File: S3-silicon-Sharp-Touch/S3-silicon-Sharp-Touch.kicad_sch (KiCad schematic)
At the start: 63 parts, among them IC1 ESP32-S3FN8, J2 Conn_01x06_Socket, J3 Conn_01x11_Socket, J5 FH52-10S-0.5SH_99, J6 5024260810, J7 S2B-PH-SM4-TB_LF__SN_, J9 USB_C_Receptacle_USB2.0, Q3 MMBT3904, Q3 Si2301CDS, Q4 MMBT3904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

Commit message: Heading for Rel 1.1
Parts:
- added J4: SM04B-SRSS-TB_LF__SN_, foot_sharp:QWIIC_SM04B-SRSS-TB_LFSN_, symbol QWIIC:SM04B-SRSS-TB_LF__SN_
- D8: value LED -> LED GREEN
- D9: value LED -> LED RED
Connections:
- net GND: now also J7.1, J4.4; no longer J7.2
- net SCL: now also J4.1
- net SDA: now also J4.2
- net VBAT: now also J7.2; no longer J7.1
- net VDD33: now also J4.3
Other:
- note added: "QWIIC I2C Connector"
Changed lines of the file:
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@@
     (stroke (width 0) (type default))
   )
+  (wire (pts (xy 344.17 106.68) (xy 336.55 106.68))
+    (stroke (width 0) (type default))
+  )
   (wire (pts (xy 336.55 166.37) (xy 340.36 166.37))
     (stroke (width 0) (type default))
@@
     (stroke (width 0) (type default))
   )
+  (wire (pts (xy 344.17 110.49) (xy 344.17 106.68))
+    (stroke (width 0) (type default))
+  )
   (wire (pts (xy 156.21 97.79) (xy 161.29 97.79))
     (stroke (width 0) (type default))
@@
     (stroke (width 0) (type default))
   )
+  (wire (pts (xy 264.16 229.87) (xy 264.16 228.6))
+    (stroke (width 0) (type default))
+  )
   (wire (pts (xy 85.09 147.32) (xy 85.09 149.86))
     (stroke (width 0) (type default))
@@
     (stroke (width 0) (type default))
   )
+  (rectangle (start 233.68 209.55) (end 316.23 242.57)
+    (stroke (width 0) (type default))
+    (fill (type none))
+  )
   (rectangle (start 318.77 146.05) (end 383.54 199.39)
     (stroke (width 0) (type default))
@@
     (effects (font (size 1.27 1.27)) (justify left bottom))
   )
+  (text "QWIIC I2C Connector" (at 234.95 208.28 0)
+    (effects (font (size 1.27 1.27)) (justify left bottom))
+  )
   (text "R2 intentionally\nNOT placed" (at 45.72 119.38 0)
     (effects (font (size 1.27 1.27)) (justify left bottom))
@@
     (effects (font (size 0.9 0.9)) (justify left bottom))
   )
-  (text "10 FPC SHARP LCD connector" (at 252.73 146.05 0)
-    (effects (font (size 2 2)) (justify left bottom))
+  (text "10 FPC SHARP LCD connector" (at 236.22 144.78 0)
+    (effects (font (size 1.27 1.27) (thickness 0.254) bold) (justify left bottom))
   )
   (text "RC delay" (at 156.21 93.98 0)
@@
     (effects (font (size 1.27 1.27) (thickness 0.254) bold (color 0 194 0 1)) (justify right bottom))
   )
+  (label "SDA" (at 264.16 223.52 180) (fields_autoplaced)
+    (effects (font (size 1.27 1.27)) (justify right bottom))
+  )
   (label "RTC_SQW" (at 97.79 48.26 0) (fields_autoplaced)
     (effects (font (size 1.27 1.27)) (justify left bottom))
@@
     (effects (font (size 1.27 1.27)) (justify right bottom))
   )
+  (label "SCL" (at 264.16 220.98 180) (fields_autoplaced)
+    (effects (font (size 1.27 1.27)) (justify right bottom))
+  )
   (label "LCD_EXTMODE" (at 273.05 175.26 180) (fields_autoplaced)
     (effects (font (size 1.27 1.27) (thickness 0.254) bold (color 72 72 72 1)) (justify right bottom))
@@
     )
   )
-  (global_label "VBAT" (shape input) (at 336.55 106.68 0) (fields_autoplaced)
-    (effects (font (size 1.27 1.27)) (justify left))
-    (property "Intersheetrefs" "${INTERSHEET_REFS}" (at 343.95 106.68 0)
-      (effects (font (size 1.27 1.27)) (justify left) hide)
-    )
-  )
   (global_label "VBUS" (shape input) (at 309.88 48.26 180) (fields_autoplaced)
     (effects (font (size 1.27 1.27)) (justify right))
@@
     )
   )
+  (global_label "VDD33" (shape input) (at 264.16 226.06 180) (fields_autoplaced)
+    (effects (font (size 1.27 1.27)) (justify right))
+    (property "Intersheetrefs" "${INTERSHEET_REFS}" (at 255.1272 226.06 0)
+      (effects (font (size 1.27 1.27)) (justify right) hide)
+    )
+    (property "Referenzen zwischen Schaltplänen" "${INTERSHEET_REFS}" (at 264.16 228.2508 0)
+      (effects (font (size 1.27 1.27)) (justify right) hide)
+    )
+  )
   (global_label "VDD33" (shape input) (at 87.63 78.74 0) (fields_autoplaced)
     (effects (font (size 1.27 1.27)) (justify left))
@@
     )
   )
+  (global_label "VBAT" (shape input) (at 336.55 109.22 0) (fields_autoplaced)
+    (effects (font (size 1.27 1.27)) (justify left))
+    (property "Intersheetrefs" "${INTERSHEET_REFS}" (at 343.95 109.22 0)
+      (effects (font (size 1.27 1.27)) (justify left) hide)
+    )
+  )
   (global_label "VBAT" (shape input) (at 323.85 69.85 180) (fields_autoplaced)
     (effects (font (size 1.27 1.27)) (justify right))
@@
       (effects (font (size 1.27 1.27)) (justify right))
     )
-    (property "Value" "LED" (at 275.59 90.17 0)
+    (property "Value" "LED GREEN" (at 275.59 90.17 0)
       (effects (font (size 1.27 1.27) (color 0 132 0 1)) (justify right))
     )
@@
       (effects (font (size 1.27 1.27)) (justify right))
     )
-    (property "Value" "LED" (at 275.59 97.79 0)
+    (property "Value" "LED RED" (at 275.59 97.79 0)
       (effects (font (size 1.27 1.27) (color 194 0 0 1)) (justify right))
     )
@@
     )
   )
+  (symbol (lib_id "power:GND") (at 264.16 229.87 0) (unit 1)
+    (in_bom yes) (on_board yes) (dnp no)
+    (property "Reference" "#PWR034" (at 264.16 236.22 0)
+      (effects (font (size 1.27 1.27)) hide)
+    )
+    (property "Value" "GND" (at 264.287 234.2642 0)
+      (effects (font (size 1.27 1.27)))
+    )
+    (property "Footprint" "" (at 264.16 229.87 0)
+      (effects (font (size 1.27 1.27)) hide)
+    )
+    (property "Datasheet" "" (at 264.16 229.87 0)
+      (effects (font (size 1.27 1.27)) hide)
+    )
+    (pin "1")
+    (instances
+      (project "S3-silicon-Sharp-Touch"
+        (path "/e6751642-eada-4b92-b3bd-08d265514654"
+          (reference "#PWR034") (unit 1)
+        )
+      )
+    )
+  )
   (symbol (lib_id "power:GND") (at 167.64 82.55 0) (unit 1)
     (in_bom yes) (on_board yes) (dnp no) (fields_autoplaced)
@@
     )
   )
+  (symbol (lib_id "QWIIC:SM04B-SRSS-TB_LF__SN_") (at 264.16 220.98 0) (unit 1)
+    (in_bom yes) (on_board yes) (dnp no) (fields_autoplaced)
+    (property "Reference" "J4" (at 280.162 222.9429 0)
+      (effects (font (size 1.27 1.27)) (justify left))
+    )
+    (property "Value" "SM04B-SRSS-TB_LF__SN_" (at 280.162 225.3671 0)
+      (effects (font (size 1.27 1.27)) (justify left))
+    )
+    (property "Footprint" "foot_sharp:QWIIC_SM04B-SRSS-TB_LFSN_" (at 280.67 315.9 0)
+      (effects (font (size 1.27 1.27)) (justify left top) hide)
+    )
+    (property "Datasheet" "http://www.jst-mfg.com/product/pdf/eng/eSH.pdf" (at 280.67 415.9 0)
+      (effects (font (size 1.27 1.27)) (justify left top) hide)
+    )
+    (property "Height" "" (at 280.67 615.9 0)
+      (effects (font (size 1.27 1.27)) (justify left top) hide)
+    )
+    (property "Manufacturer_Name" "JST (JAPAN SOLDERLESS TERMINALS)" (at 280.67 715.9 0)
+      (effects (font (size 1.27 1.27)) (justify left top) hide)
+    )
+    (property "Manufacturer_Part_Number" "SM04B-SRSS-TB(LF)(SN)" (at 280.67 815.9 0)
+      (effects (font (size 1.27 1.27)) (justify left top) hide)
+    )
+    (property "Mouser Part Number" "" (at 280.67 915.9 0)
+      (effects (font (size 1.27 1.27)) (justify left top) hide)
+    )
+    (property "Mouser Price/Stock" "" (at 280.67 1015.9 0)
+      (effects (font (size 1.27 1.27)) (justify left top) hide)
+    )
+    (property "Arrow Part Number" "SM04B-SRSS-TB(LF)(SN)" (at 280.67 1115.9 0)
+      (effects (font (size 1.27 1.27)) (justify left top) hide)
+    )
+    (property "Arrow Price/Stock" "https://www.arrow.com/en/products/sm04b-srss-tb-lf-sn/jst-manufacturing?region=europe" (at 280.67 1215.9 0)
+      (effects (font (size 1.27 1.27)) (justify left top) hide)
+    )
+    (property "LCSC" "C160404" (at 264.16 220.98 90)
+      (effects (font (size 1.27 1.27)) hide)
+    )
+    (pin "4")
+    (pin "2")
+    (pin "3")
+    (pin "1")
+    (pin "6")
+    (pin "5")
+    (instances
+      (project "S3-silicon-Sharp-Touch"
+        (path "/e6751642-eada-4b92-b3bd-08d265514654"
+          (reference "J4") (unit 1)
+        )
+      )
+    )
+  )
   (symbol (lib_id "Device:R") (at 115.57 156.21 270) (unit 1)
     (in_bom yes) (on_board yes) (dnp no)
@@
     )
   )
+  (symbol (lib_id "power:GND") (at 344.17 110.49 0) (unit 1)
+    (in_bom yes) (on_board yes) (dnp no) (fields_autoplaced)
+    (property "Reference" "#PWR05" (at 344.17 116.84 0)
+      (effects (font (size 1.27 1.27)) hide)
+    )
+    (property "Value" "GND" (at 344.17 115.0525 0)
+      (effects (font (size 1.27 1.27)))
+    )
+    (property "Footprint" "" (at 344.17 110.49 0)
+      (effects (font (size 1.27 1.27)) hide)
+    )
+    (property "Datasheet" "" (at 344.17 110.49 0)
+      (effects (font (size 1.27 1.27)) hide)
+    )
+    (pin "1")
+    (instances
+      (project "S3-silicon-Sharp-Touch"
+        (path "/e6751642-eada-4b92-b3bd-08d265514654"
+          (reference "#PWR05") (unit 1)
+        )
+      )
+    )
+  )
   (symbol (lib_id "power:GND") (at 265.43 179.07 0) (unit 1)
     (in_bom yes) (on_board yes) (dnp no) (fields_autoplaced)
@@
         )
       )
-    )
-  )
-  (symbol (lib_id "power:GND") (at 336.55 109.22 0) (unit 1)
-    (in_bom yes) (on_board yes) (dnp no) (fields_autoplaced)
-    (property "Reference" "#PWR034" (at 336.55 115.57 0)
-      (effects (font (size 1.27 1.27)) hide)
-    )
-    (property "Value" "GND" (at 336.55 113.7825 0)
-      (effects (font (size 1.27 1.27)))
-    )
-    (property "Footprint" "" (at 336.55 109.22 0)
-      (effects (font (size 1.27 1.27)) hide)
-    )
-    (property "Datasheet" "" (at 336.55 109.22 0)
-      (effects (font (size 1.27 1.27)) hide)
-    )
-    (pin "1")
-    (instances
-      (project "S3-silicon-Sharp-Touch"
-        (path "/e6751642-eada-4b92-b3bd-08d265514654"
-          (reference "#PWR034") (unit 1)
-        )
-      )

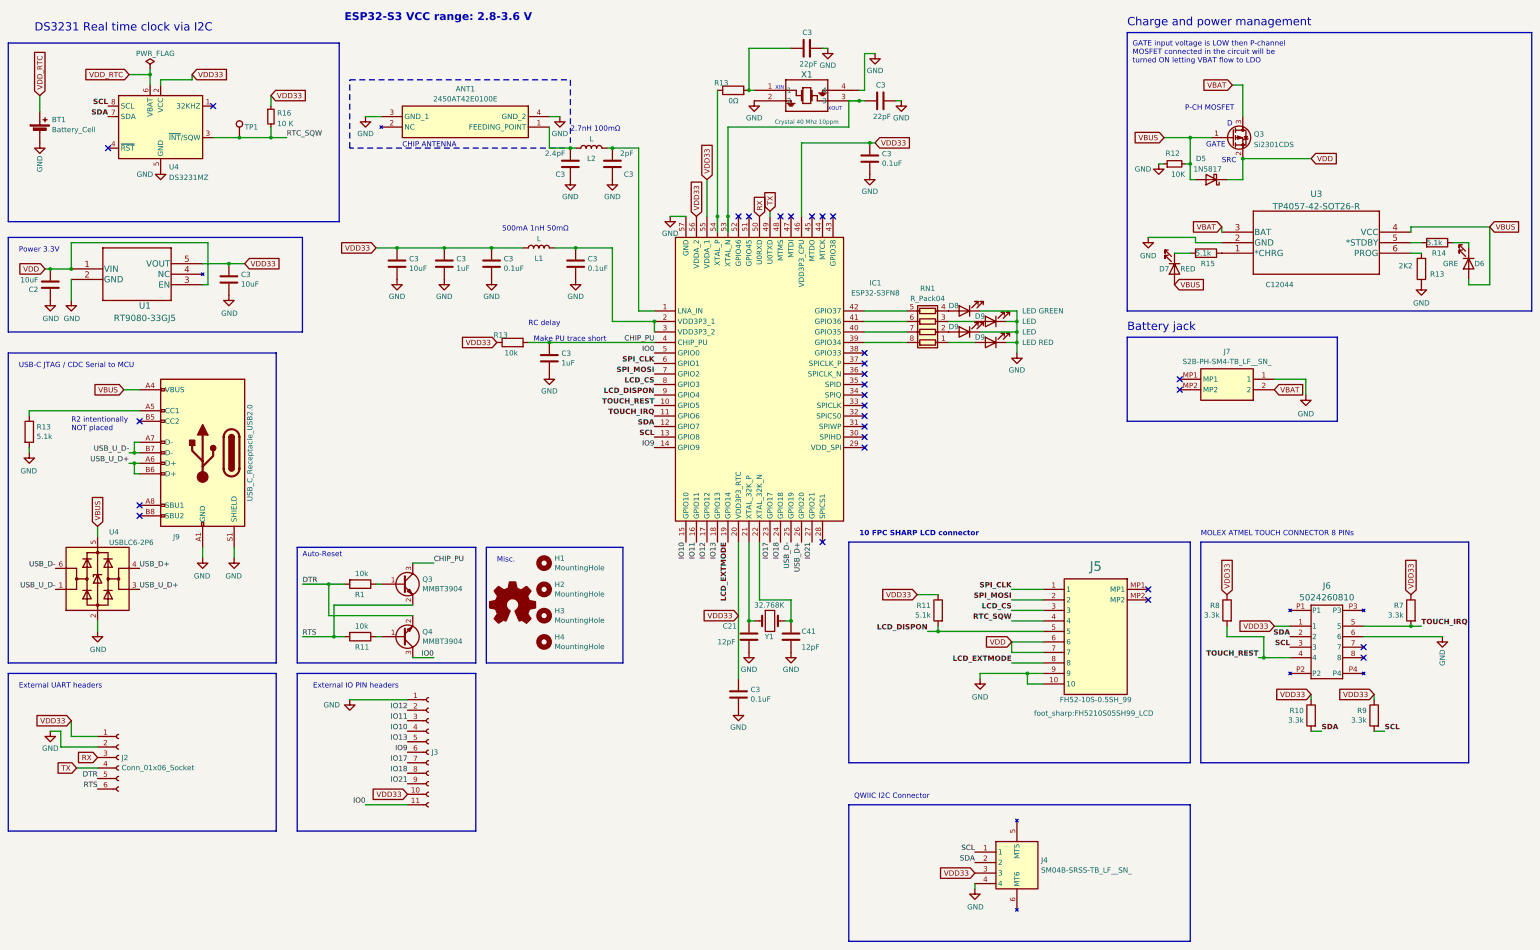
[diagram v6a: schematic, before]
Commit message: Update RTC with RV-3032
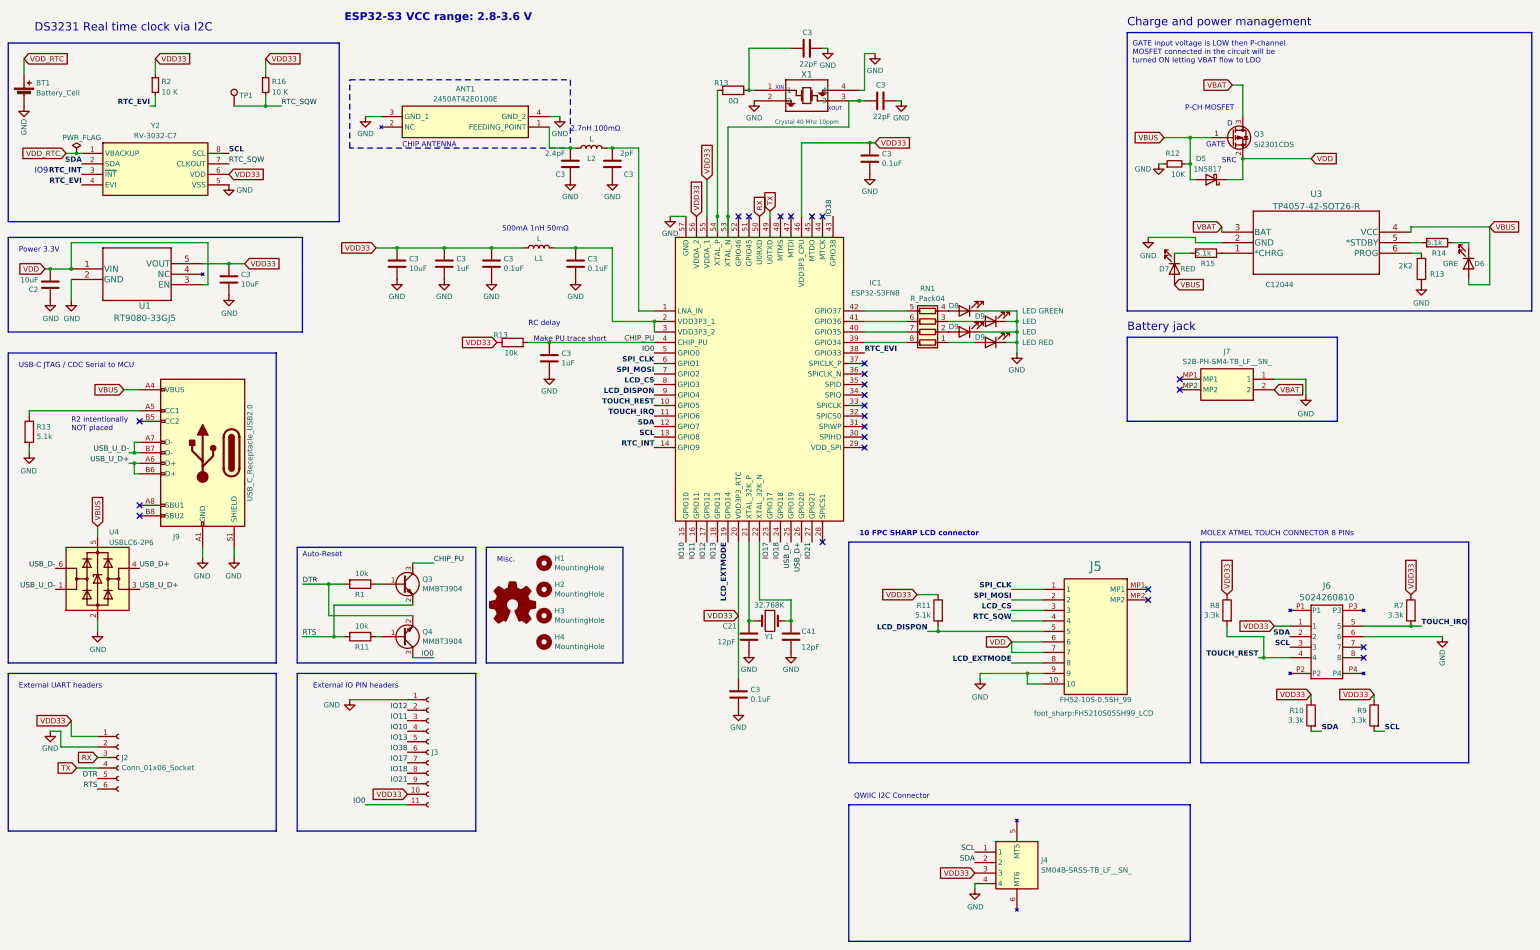
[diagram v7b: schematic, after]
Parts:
- removed U4: DS3231MZ, Package_SO:SOIC-8_3.9x4.9mm_P1.27mm, symbol Timer_RTC:DS3231MZ
- added R2: 10 K, Resistor_SMD:R_0603_1608Metric, symbol Device:R_Small
- added Y2: RV-3032-C7, RV3032C7, symbol RTC:RV-3032-C7
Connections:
- net GND: now also Y2.5 (VSS)
- net RTC_SQW: now also Y2.7 (CLKOUT)
- net SCL: now also Y2.8 (SCL)
- net SDA: now also Y2.2 (SDA)
- net VDD33: now also R2.1, Y2.6 (VDD)
- net VDD_RTC: now also Y2.1 (VBACKUP)
- net RTC_EVI: now reaches IC1.38 (GPIO33)
- net RTC_EVI: now also R2.2, Y2.4 (EVI)
- net IO38: now reaches IC1.43 (GPIO38)
- net IO38: now also J3.6 (Pin_6)
- net IO9 renamed RTC_INT
- net RTC_INT: now also Y2.3 (~{INT}); no longer J3.6 (Pin_6)
- no-connect marks 29 -> 25
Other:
- note added: "IO9"
- moved on the sheet: BT1, R16, TP1

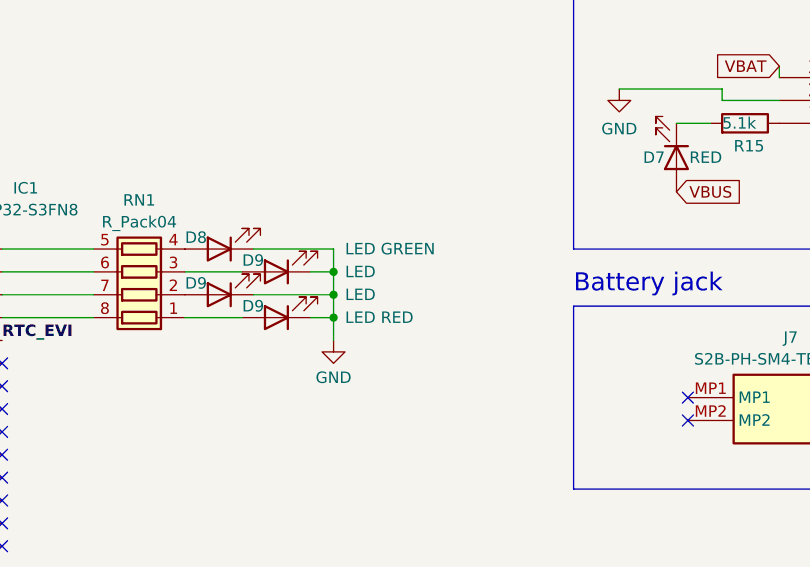
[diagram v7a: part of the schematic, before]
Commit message: 1.1 cut-outs
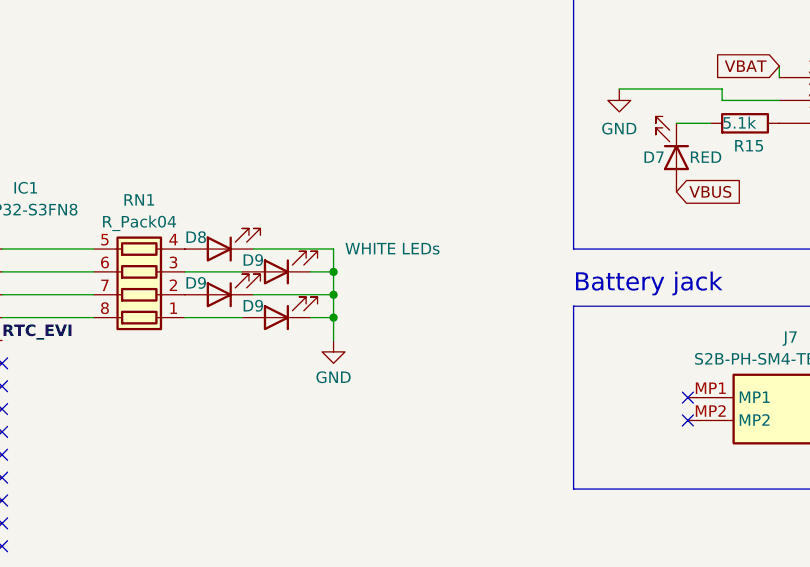
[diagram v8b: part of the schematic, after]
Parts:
- D8: value LED GREEN -> WHITE LEDs; footprint LED_SMD:LED_0805_2012Metric -> LED_SMD:LED_0603_1608Metric; LCSC C2297 -> C575431
- D9: footprint LED_SMD:LED_0805_2012Metric -> LED_SMD:LED_0603_1608Metric; LCSC C84256 -> C575431
- D9: footprint LED_SMD:LED_0805_2012Metric -> LED_SMD:LED_0603_1608Metric; LCSC C2297 -> C575431
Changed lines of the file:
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@@
       (effects (font (size 1.27 1.27)) (justify right))
     )
-    (property "Value" "LED GREEN" (at 275.59 90.17 0)
+    (property "Value" "WHITE LEDs" (at 275.59 90.17 0)
       (effects (font (size 1.27 1.27) (color 0 132 0 1)) (justify right))
     )
-    (property "Footprint" "LED_SMD:LED_0805_2012Metric" (at 261.62 90.17 0)
+    (property "Footprint" "LED_SMD:LED_0603_1608Metric" (at 261.62 90.17 0)
       (effects (font (size 1.27 1.27)) hide)
     )
@@
       (effects (font (size 1.27 1.27)) hide)
     )
-    (property "LCSC" "C2297" (at 261.62 90.17 90)
+    (property "LCSC" "C575431" (at 261.62 90.17 90)
       (effects (font (size 1.27 1.27)) hide)
     )
@@
     )
     (property "Value" "LED RED" (at 275.59 97.79 0)
-      (effects (font (size 1.27 1.27) (color 194 0 0 1)) (justify right))
-    )
-    (property "Footprint" "LED_SMD:LED_0805_2012Metric" (at 267.97 97.79 0)
+      (effects (font (size 1.27 1.27) (color 194 0 0 1)) (justify right) hide)
+    )
+    (property "Footprint" "LED_SMD:LED_0603_1608Metric" (at 267.97 97.79 0)
       (effects (font (size 1.27 1.27)) hide)
     )
@@
       (effects (font (size 1.27 1.27)) hide)
     )
-    (property "LCSC" "C84256" (at 267.97 97.79 90)
+    (property "LCSC" "C575431" (at 267.97 97.79 90)
       (effects (font (size 1.27 1.27)) hide)
     )
@@
     )
     (property "Value" "LED" (at 275.59 95.25 0)
-      (effects (font (size 1.27 1.27) (color 194 0 0 1)) (justify right))
-    )
-    (property "Footprint" "LED_SMD:LED_0805_2012Metric" (at 261.62 95.25 0)
+      (effects (font (size 1.27 1.27) (color 194 0 0 1)) (justify right) hide)
+    )
+    (property "Footprint" "LED_SMD:LED_0603_1608Metric" (at 261.62 95.25 0)
       (effects (font (size 1.27 1.27)) hide)
     )
@@
       (effects (font (size 1.27 1.27)) hide)
     )
-    (property "LCSC" "C84256" (at 261.62 95.25 90)
+    (property "LCSC" "C575431" (at 261.62 95.25 90)
       (effects (font (size 1.27 1.27)) hide)
     )
@@
     )
     (property "Value" "LED" (at 275.59 92.71 0)
-      (effects (font (size 1.27 1.27) (color 0 132 0 1)) (justify right))
-    )
-    (property "Footprint" "LED_SMD:LED_0805_2012Metric" (at 267.97 92.71 0)
+      (effects (font (size 1.27 1.27) (color 0 132 0 1)) (justify right) hide)
+    )
+    (property "Footprint" "LED_SMD:LED_0603_1608Metric" (at 267.97 92.71 0)
       (effects (font (size 1.27 1.27)) hide)
     )
@@
       (effects (font (size 1.27 1.27)) hide)
     )
-    (property "LCSC" "C2297" (at 267.97 92.71 90)
-      (effects (font (size 1.27 1.27)) hide)
-    )
+    (property "LCSC" "C575431" (at 267.97 92.71 90)
+      (effects (font (size 1.27 1.27)) hide)
+    )
